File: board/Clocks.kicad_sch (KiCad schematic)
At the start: 28 parts, among them J15 AudioJack3, J17 Front Panel, J4 7.15909MHz, J5 ATX-24, J6 0.89488625MHz, J7 1.7897725MHz, J8 3.579545MHz, U36 74ACT14, U37 74F191, U38 TL074, U39 YM2151, U40 YM3012, U41 DM1813-10, Y1 14.31818MHz

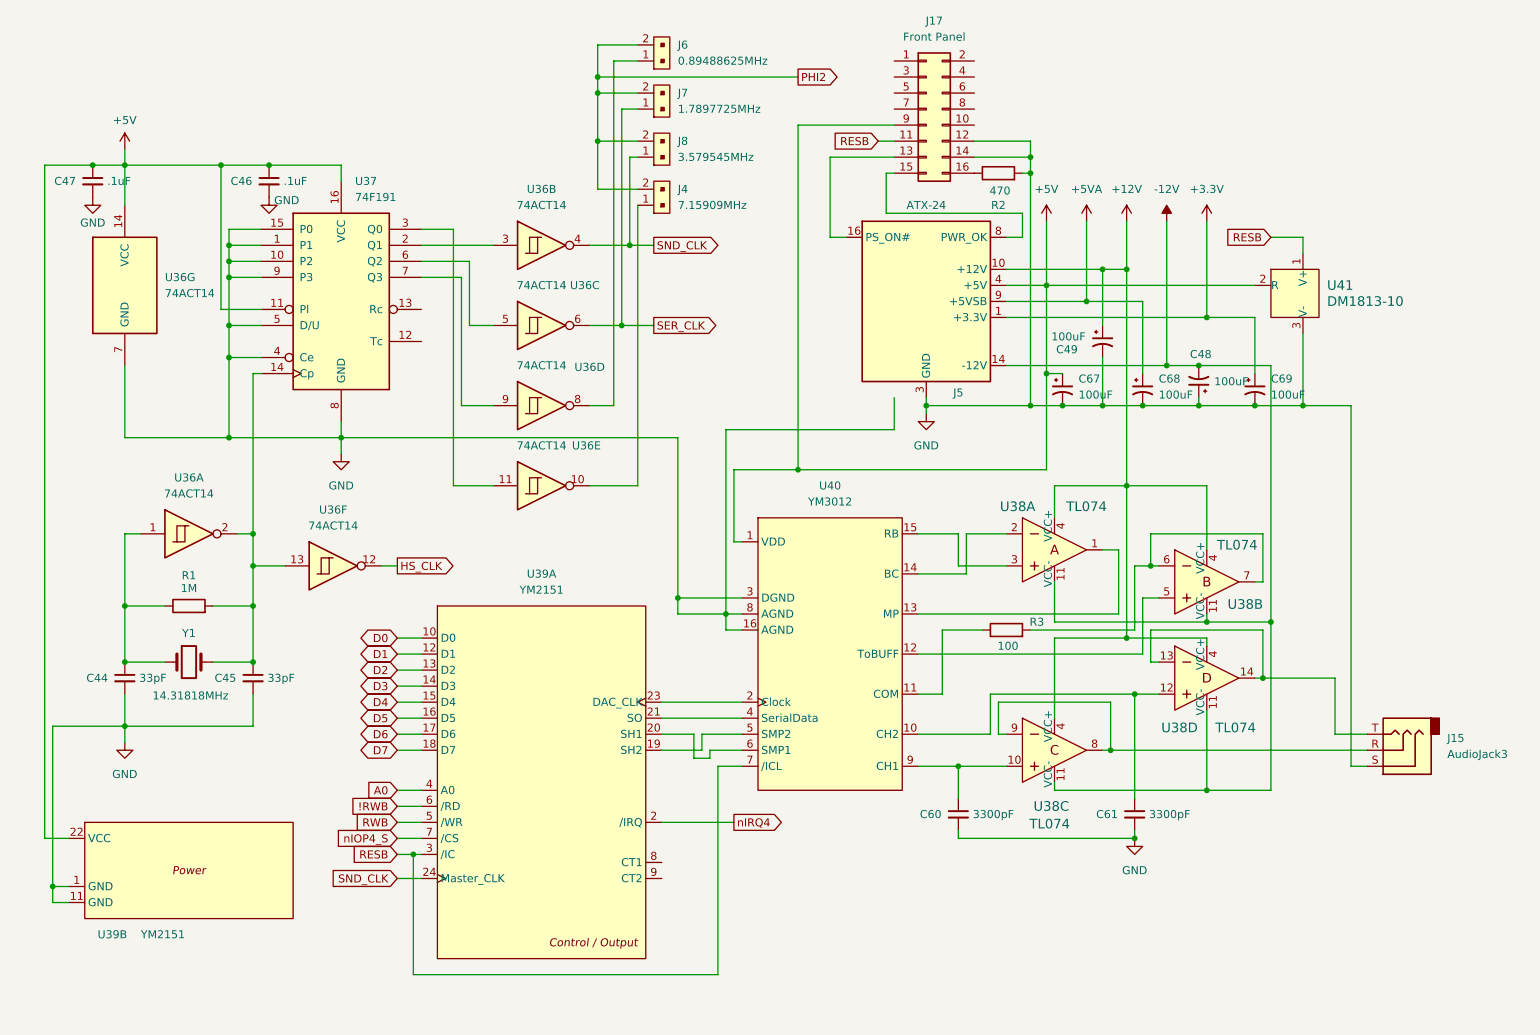
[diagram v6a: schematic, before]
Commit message: Schematic Bus updates, silkscreen updates, position tweaks, and other corrections.
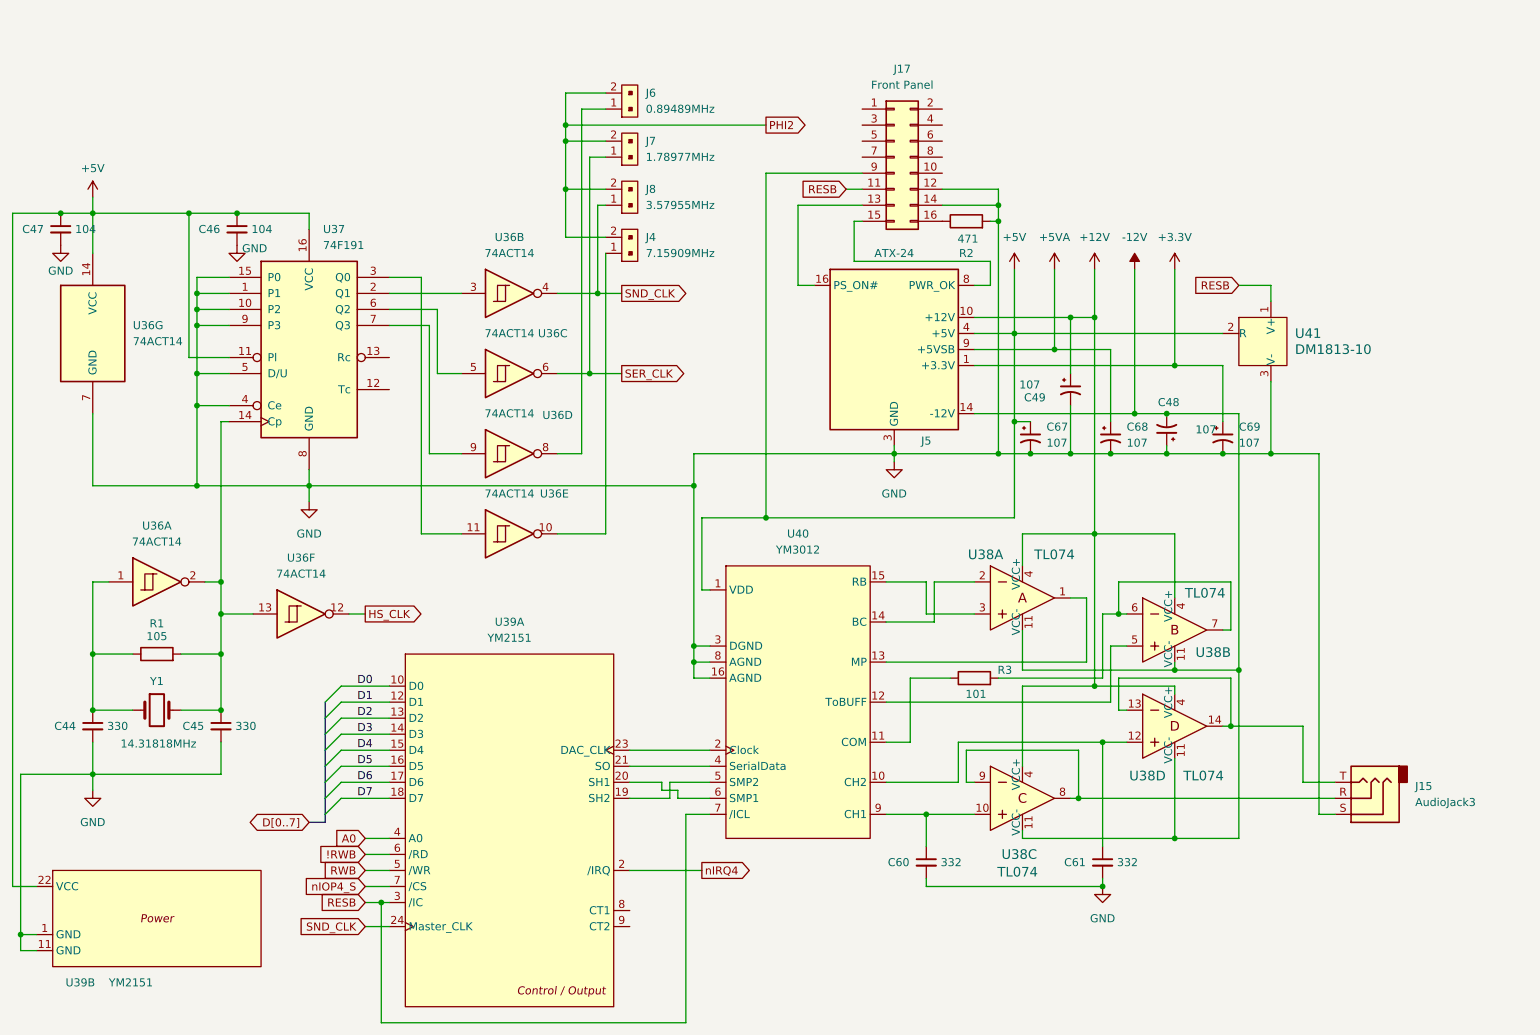
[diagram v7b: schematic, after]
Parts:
- C44, C45: value 33pF -> 330
- C46, C47: value .1uF -> 104; footprint Capacitor_THT:C_Disc_D5.0mm_W2.5mm_P2.50mm -> Capacitor_THT:C_Disc_D5.0mm_W2.5mm_P5.00mm
- C48, C49, C67, C68, C69: value 100uF -> 107
- C60, C61: value 3300pF -> 332
- J6: value 0.89488625MHz -> 0.89489MHz
- J7: value 1.7897725MHz -> 1.78977MHz
- J8: value 3.579545MHz -> 3.57955MHz
- R1: value 1M -> 105
- R2: value 470 -> 471
- R3: value 100 -> 101
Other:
- company: (none) -> Data Tuning
- title: (none) -> Sound, Clocks, and Power
- moved on the sheet: C44, C45, C46, C47, C48, C49, C60, C61, C67, C68, C69, J15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

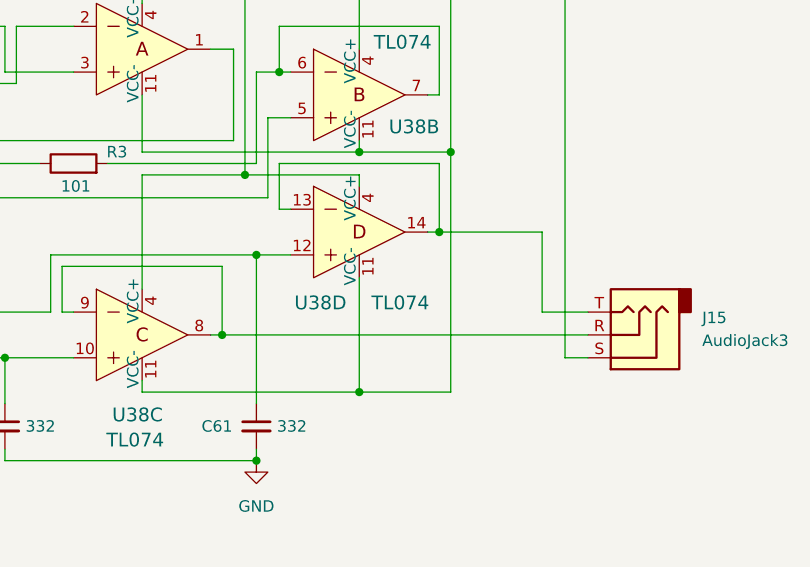
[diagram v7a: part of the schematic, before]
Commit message: Moving external resources into source.
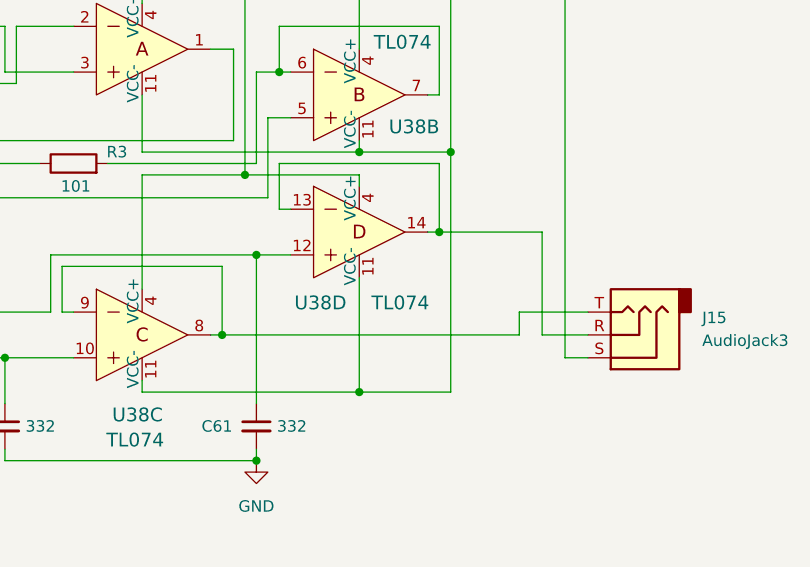
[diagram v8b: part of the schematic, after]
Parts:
- J15: footprint Connector_Audio:Jack_3.5mm_CUI_SJ1-3524N_Horizontal -> Connector_Audio:Jack_3.5mm_CUI_SJ1-3523N_Horizontal
- J5: footprint MolexATX24:CON_39299247 -> Connector_Molex:Molex_Mini-Fit_Jr_5566-24A2_2x12_P4.20mm_Vertical
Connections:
- net at U38.13, U38.14: now also J15.R; no longer J15.T
- net at U38.8, U38.9: now also J15.T; no longer J15.R
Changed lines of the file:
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@@
 	(wire
 		(pts
-			(xy 196.85 138.43) (xy 237.49 138.43)
+			(xy 196.85 138.43) (xy 229.87 138.43)
 		)
 		(stroke
@@
 	(wire
 		(pts
-			(xy 237.49 135.89) (xy 232.41 135.89)
-		)
-		(stroke
-			(width 0)
-			(type default)
-		)
-	)
-	(wire
-		(pts
 			(xy 137.16 105.41) (xy 137.16 93.98)
 		)
@@
 	(wire
 		(pts
+			(xy 229.87 135.89) (xy 237.49 135.89)
+		)
+		(stroke
+			(width 0)
+			(type default)
+		)
+	)
+	(wire
+		(pts
 			(xy 179.07 135.89) (xy 179.07 130.81)
 		)
@@
 	(wire
 		(pts
+			(xy 229.87 135.89) (xy 229.87 138.43)
+		)
+		(stroke
+			(width 0)
+			(type default)
+		)
+	)
+	(wire
+		(pts
 			(xy 86.36 173.99) (xy 134.62 173.99)
 		)
@@
 	(wire
 		(pts
-			(xy 232.41 135.89) (xy 232.41 127)
+			(xy 232.41 127) (xy 232.41 138.43)
 		)
 		(stroke
@@
 	(wire
 		(pts
+			(xy 232.41 138.43) (xy 237.49 138.43)
+		)
+		(stroke
+			(width 0)
+			(type default)
+		)
+	)
+	(wire
+		(pts
 			(xy 135.89 116.84) (xy 138.43 116.84)
 		)
@@
 			)
 		)
-		(property "Footprint" "Connector_Audio:Jack_3.5mm_CUI_SJ1-3524N_Horizontal"
+		(property "Footprint" "Connector_Audio:Jack_3.5mm_CUI_SJ1-3523N_Horizontal"
 			(at 242.57 138.43 0)
 			(effects
@@
 			)
 		)
-		(property "Footprint" "MolexATX24:CON_39299247"
+		(property "Footprint" "Connector_Molex:Molex_Mini-Fit_Jr_5566-24A2_2x12_P4.20mm_Vertical"
 			(at 167.64 69.85 0)
 			(effects
